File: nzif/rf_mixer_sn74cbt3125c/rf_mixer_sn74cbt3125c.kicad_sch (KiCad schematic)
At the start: 24 parts, among them U4 SN74CBT3125C

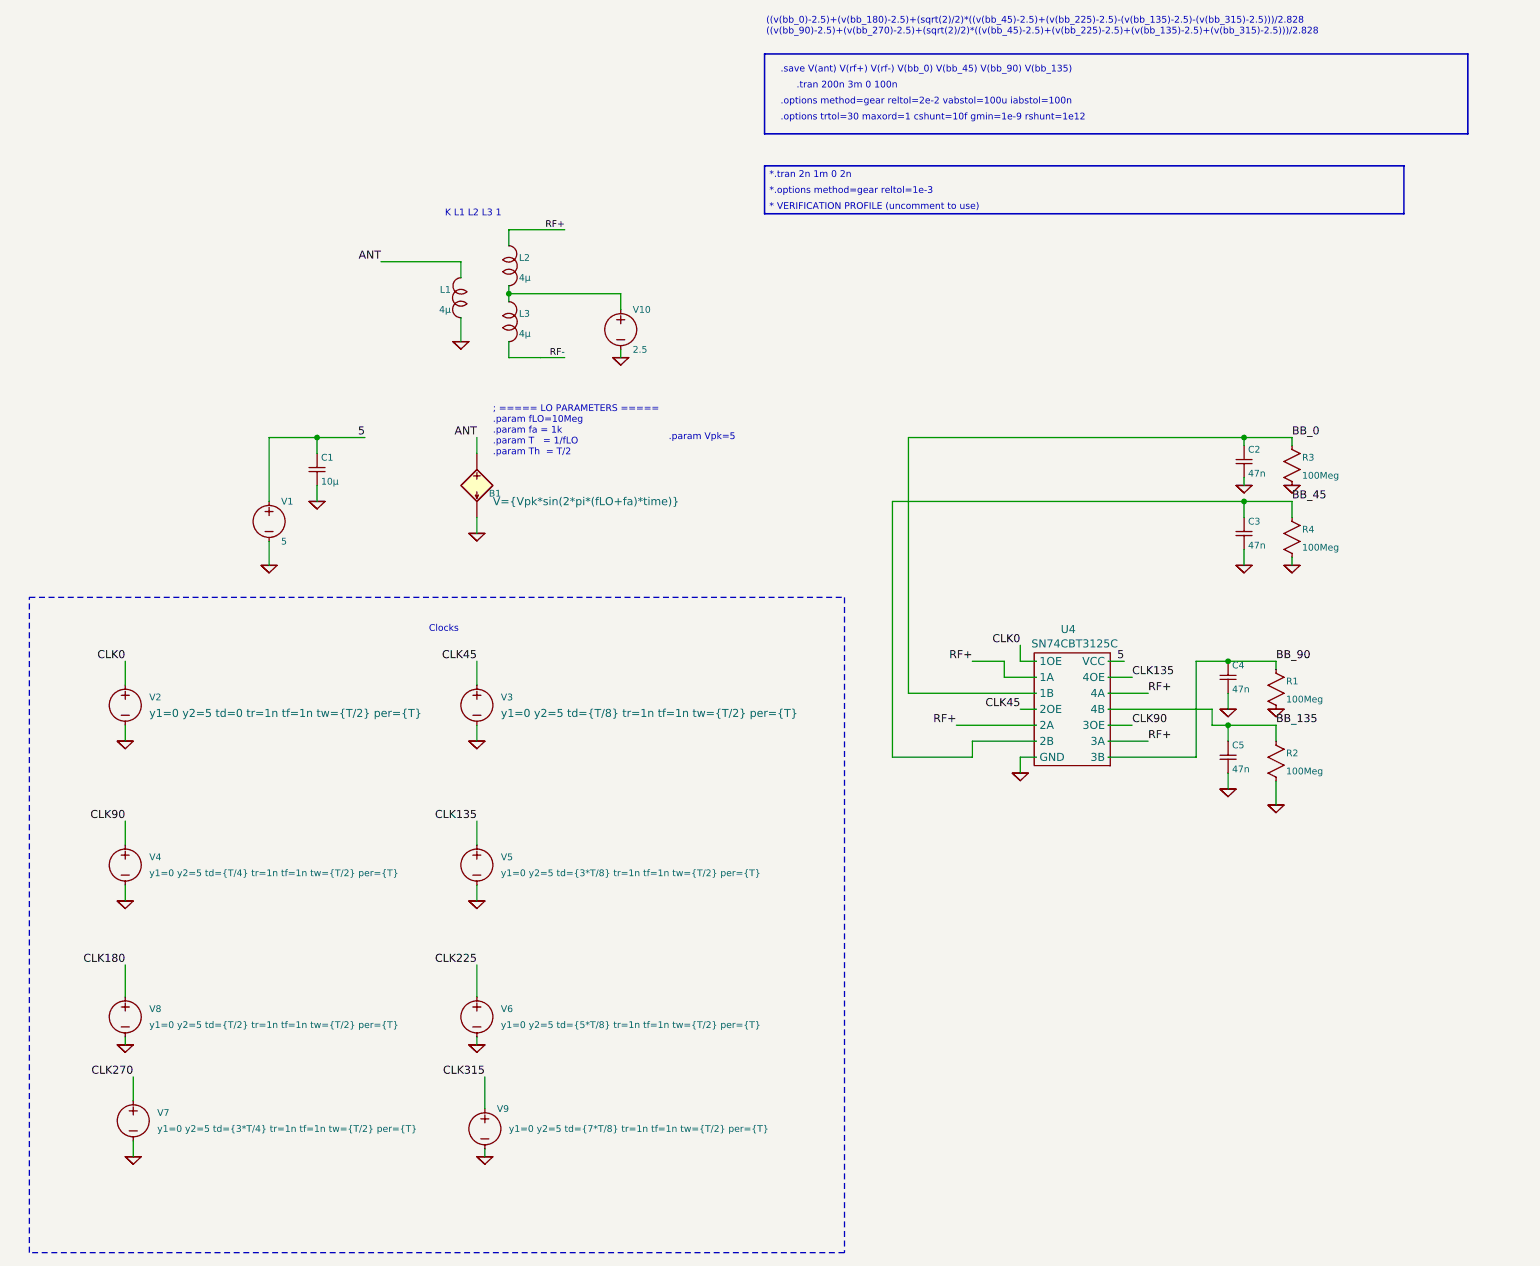
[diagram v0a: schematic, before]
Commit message: updates to rfmixer sim
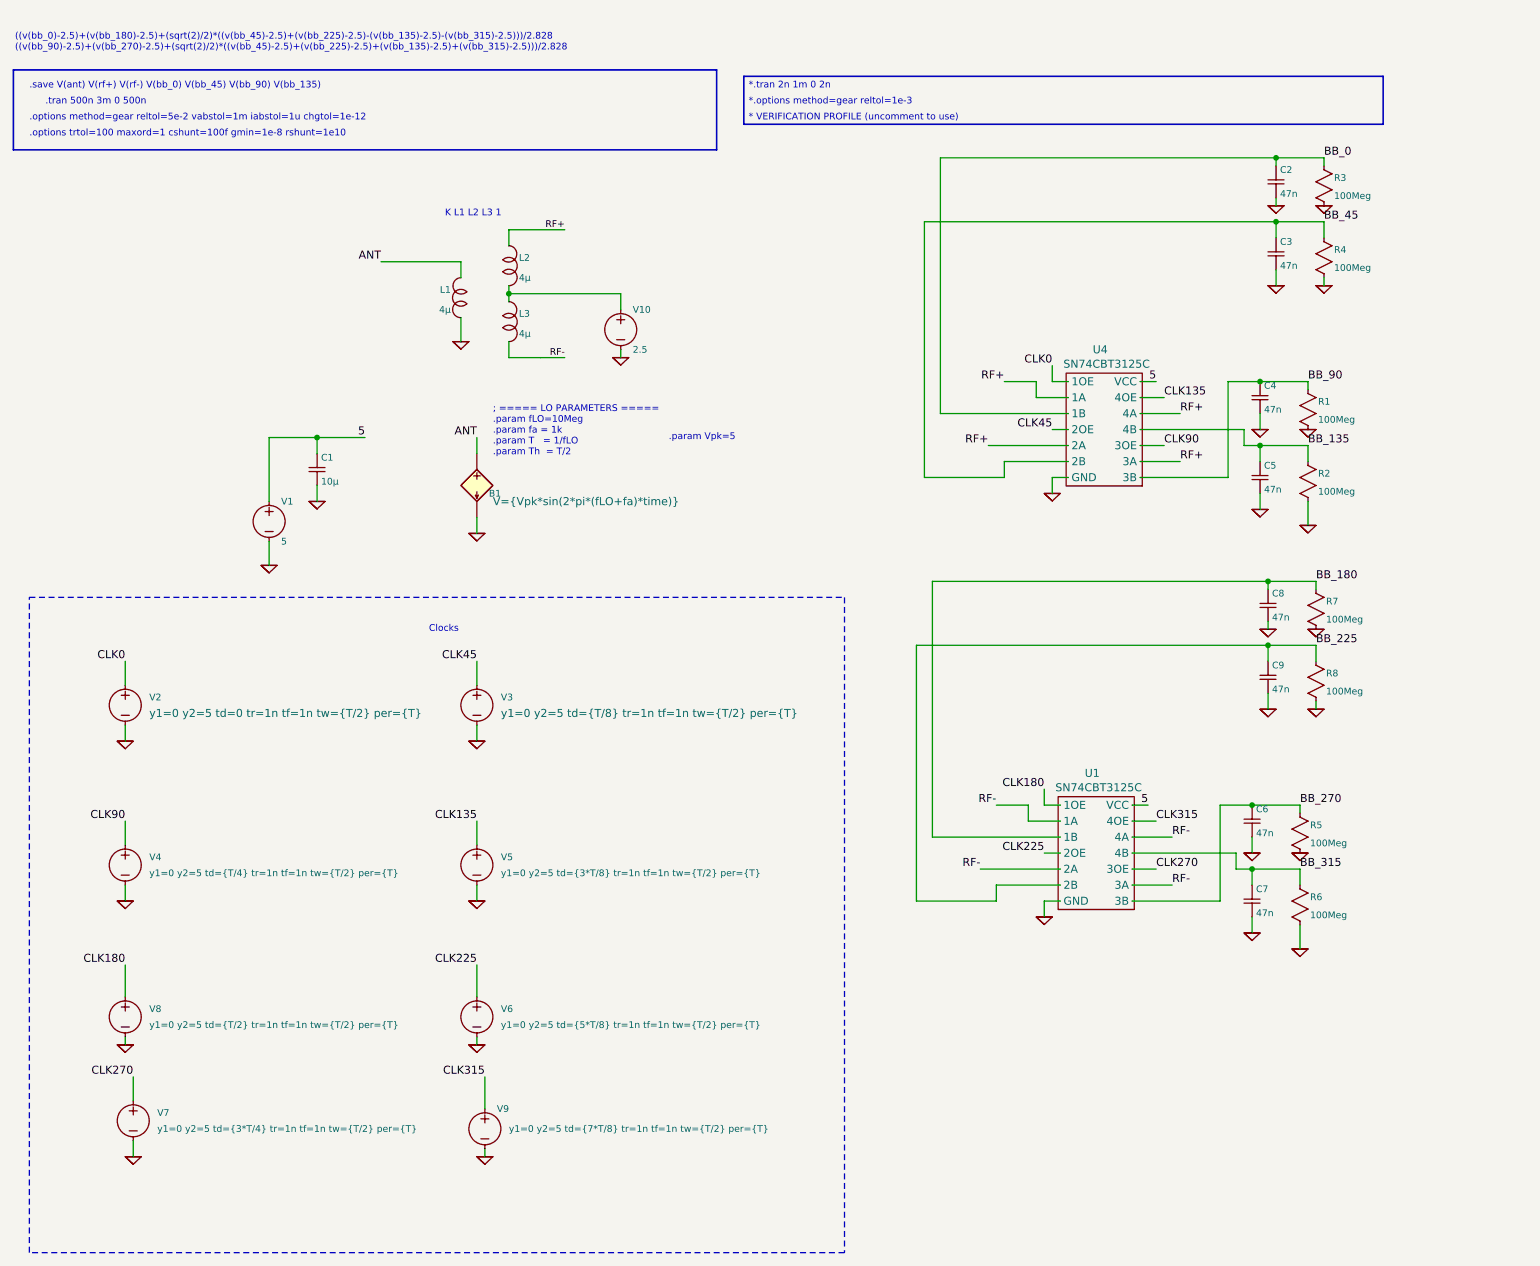
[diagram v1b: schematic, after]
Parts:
- added C6, C7, C8, C9: 47n, symbol ltspice:cap
- added R5, R6, R7, R8: 100Meg, symbol ltspice:res
- added U1: SN74CBT3125C, symbol ltspice:sn74cbt3125casy
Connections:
- net 0: now also C6.2, C7.2, C8.2, C9.2, R5.2, R6.2, R7.2, R8.2, U1.7 (GND)
- net 5: now also U1.14 (VCC)
- net CLK180: now also U1.1 (1OE)
- net CLK225: now also U1.4 (2OE)
- net CLK270: now also U1.10 (3OE)
- net CLK315: now also U1.13 (4OE)
- net RF-: now also U1.12 (4A), U1.2 (1A), U1.5 (2A), U1.9 (3A)
- new net BB_180: C8.1, R7.1, U1.3 (1B)
- new net BB_225: C9.1, R8.1, U1.6 (2B)
- new net BB_270: C6.1, R5.1, U1.8 (3B)
- new net BB_315: C7.1, R6.1, U1.11 (4B)
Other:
- note added: ".options method=gear reltol=5e-2 vabstol=1m iabstol=1u chgtol=1e-12"
- note added: ".options trtol=100 maxord=1 cshunt=100f gmin=1e-8 rshunt=1e10"
- note added: ".tran 500n 3m 0 500n"
- note removed: ".options method=gear reltol=2e-2 vabstol=100u iabstol=100n"
- note removed: ".options trtol=30 maxord=1 cshunt=10f gmin=1e-9 rshunt=1e12"
- note removed: ".tran 200n 3m 0 100n"
- moved on the sheet: C2, C3, C4, C5, R1, R2, R3, R4, U4
